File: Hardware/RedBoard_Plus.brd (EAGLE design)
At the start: 68.6 x 58.4 mm, 176 parts, among them IC3 LM1117, J2 ISP, J3 5.5x2.1mm Barrel, J4 QWIIC_RIGHT_ANGLE, J5 USB Female Type C Connector, Q1 20V/4.2A/52mΩ/1.4W, Q2 310mA/60V/1.6Ω, Q3 310mA/60V/1.6Ω, U1 CH340G, U3 3.3V, U4 ATMEGA328P_TQFP, Y1 16MHz, Y2 12MHz

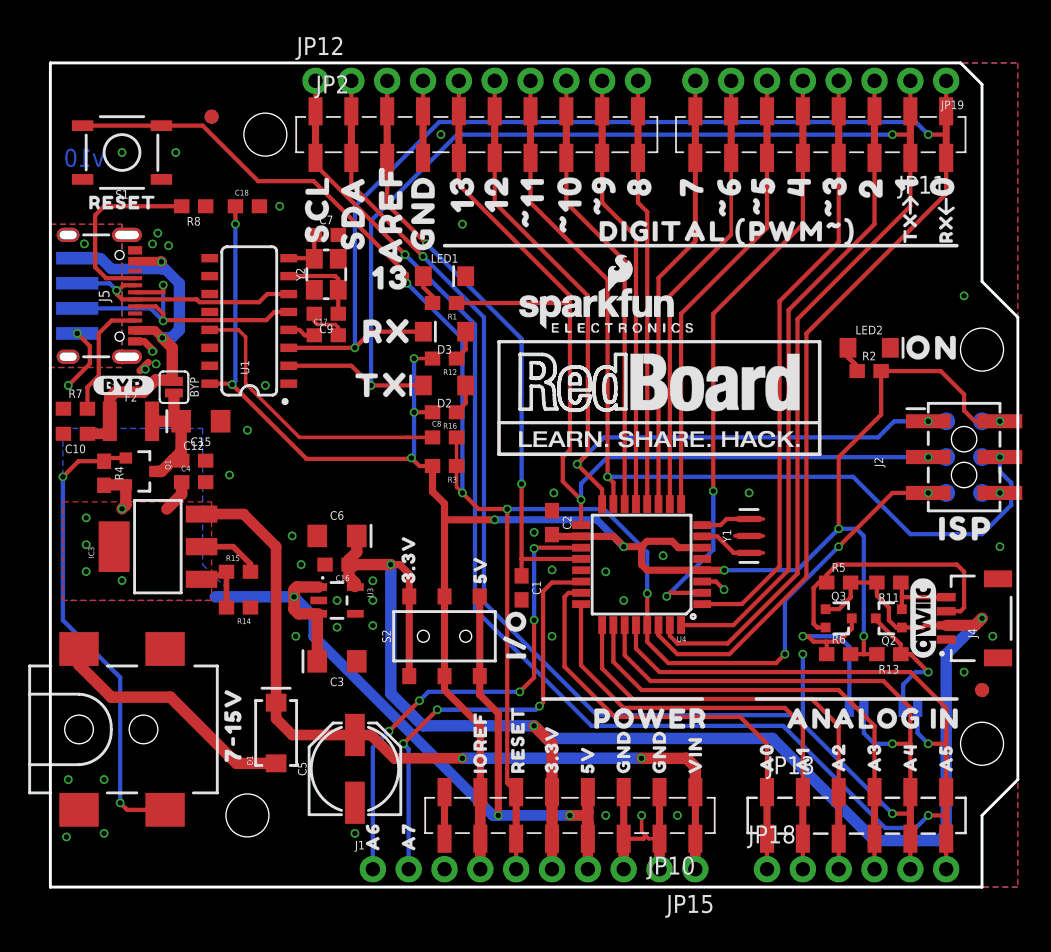
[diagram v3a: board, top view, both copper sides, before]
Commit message: Update silkscreen
Increased the size of PTH labels on back side to all be the same size
Added "(PLUS)" label to board name - top/bottom
Vector-ized "ELECTRONICS"
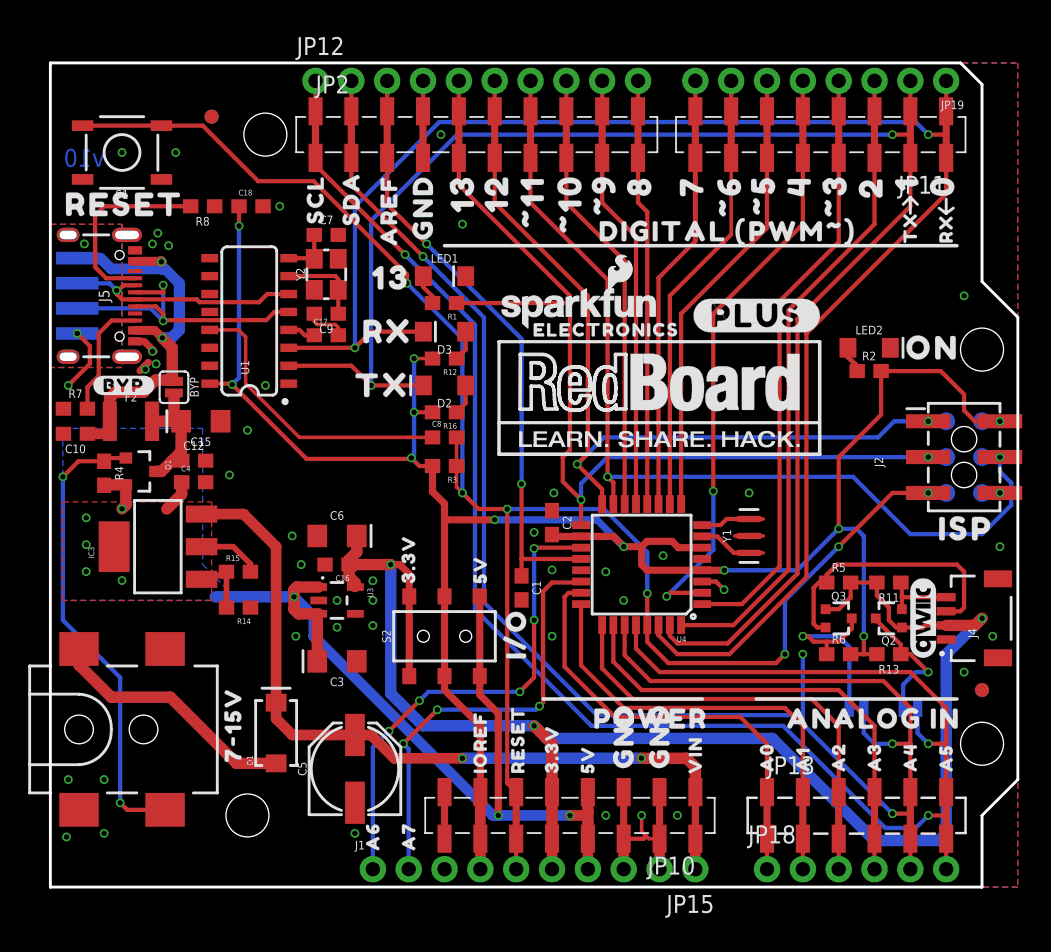
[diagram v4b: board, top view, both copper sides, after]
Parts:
- added U$102: (no value), output:_A50
- added U$103: (no value), output:#PLUS#0
- added U$104: (no value), output:ELECTRONICS0
- U$100: device output:_GND0 -> output:#PLUS#0
- U$13: device output:RESET0 -> output:_RESET0
- U$18: device output:SCL0 -> output:_AREF0
- U$19: device output:SDA0 -> output:_SCL0
- U$20: device output:AREF0 -> output:_SDA0
- U$84: device output:A40 -> output:_A40
- U$86: device output:A50 -> output:_A30
- U$87: device output:A30 -> output:_A20
- U$88: device output:A20 -> output:_A10
- U$89: device output:A10 -> output:_A00
- U$90: device output:A00 -> output:_VIN0
- U$91: device output:VIN0 -> output:_GND0
- U$92: device output:GND0 -> output:_GND0
- U$93: device output:GND0 -> output:_5V0
- U$94: device output:5V0 -> output:_3#3V0
- U$95: device output:3#3V0 -> output:_RESET0
- U$96: device output:RESET0 -> output:_IOREF0
- U$97: device output:IOREF0 -> output:_A60
- U$98: device output:A70 -> output:_A70
- U$99: device output:A60 -> output:GND0
- moved U$99 39.9 mm to (26.4, 44.8), flipped to the top, turned to 90 degrees
- moved U$100 19.4 mm to (45.6, 40.5), turned to 0 degrees
- moved U$97 7.62 mm to (22.9, 7.62)
- moved U$95 6.60 mm to (33.0, 12.7)
- moved U$90 6.35 mm to (45.7, 8.89)
- moved U$94 5.68 mm to (35.6, 10.2)
- moved U$86 5.68 mm to (58.4, 7.62)
- moved U$18 5.09 mm to (24.0, 44.2)
- moved U$91 4.76 mm to (43.1, 9.65)
- moved U$96 4.69 mm to (30.5, 11.8)
- moved U$92 4.27 mm to (40.6, 9.65)
- moved U$20 3.78 mm to (21.3, 45.6)
- moved U$89 3.78 mm to (50.8, 7.62)
- moved U$87 3.59 mm to (55.9, 7.62)
- moved U$88 3.33 mm to (53.3, 7.24)
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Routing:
- net CC1: track 13.2 -> 13.9 mm

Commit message: Run checklist
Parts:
- moved JP7 1.27 mm to (39.1, 43.6)
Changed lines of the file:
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@@
 <?xml version="1.0" encoding="utf-8"?>
 <!DOCTYPE eagle SYSTEM "eagle.dtd">
-<eagle version="9.6.2">
+<eagle version="9.5.2">
 <drawing>
 <settings>
-<setting alwaysvectorfont="yes"/>
+<setting alwaysvectorfont="no"/>
 <setting keepoldvectorfont="yes"/>
 <setting verticaltext="up"/>
@@
 <wire x1="66.04" y1="56.896" x2="66.04" y2="42.926" width="0.2032" layer="20"/>
 <text x="0" y="-0.0635" size="0.0254" layer="214" font="vector">D:/SmartProjects/Snc/a4_bn_logo2.bmp</text>
-<text x="2.413" y="51.689" size="1.27" layer="16" font="vector" ratio="20" rot="MR0" align="center">v10</text>
+<text x="2.413" y="56.769" size="1.27" layer="16" font="vector" ratio="20" rot="MR0" align="center">v10</text>
 <rectangle x1="0.635" y1="22.352" x2="2.032" y2="30.607" layer="43"/>
 <rectangle x1="5.715" y1="23.114" x2="7.366" y2="30.607" layer="43"/>
@@
 </element>
 <element name="JP1" library="SparkFun-Aesthetics" package="SFE_LOGO_NAME_.1" value="SFE_LOGO_NAME.1_INCH" x="37.465" y="41.021" smashed="yes"/>
-<element name="JP7" library="SparkFun-Aesthetics" package="SFE_LOGO_FLAME_.1" value="SFE_LOGO_FLAME.1_INCH" x="40.386" y="43.561" smashed="yes"/>
+<element name="JP7" library="SparkFun-Aesthetics" package="SFE_LOGO_FLAME_.1" value="SFE_LOGO_FLAME.1_INCH" x="39.116" y="43.561" smashed="yes"/>
 <element name="J2" library="SparkFun-Connectors" package="2X3_SMT_POSTS" value="ISP" x="64.77" y="30.48" smashed="yes" rot="R270">
 <attribute name="NAME" x="58.42" y="30.48" size="0.6096" layer="25" rot="R270"/>
@@
 <contactref element="J5" pad="B6"/>
 <contactref element="J5" pad="A6"/>
-<wire x1="6.01" y1="42.16" x2="8.005" y2="42.16" width="0.3048" layer="1"/>
 <wire x1="6.01" y1="41.16" x2="7.481" y2="41.16" width="0.3048" layer="1"/>
 <wire x1="7.481" y1="41.16" x2="8.001" y2="40.64" width="0.3048" layer="1"/>
@@
 <wire x1="8.001" y1="40.132" x2="8.001" y2="42.672" width="0.3048" layer="16"/>
 <via x="8.001" y="42.672" extent="1-16" drill="0.381"/>
-<wire x1="8.001" y1="42.672" x2="8.005" y2="42.668" width="0.3048" layer="1"/>
-<wire x1="8.005" y1="42.668" x2="8.005" y2="42.16" width="0.3048" layer="1"/>
+<wire x1="8.001" y1="42.672" x2="7.489" y2="42.16" width="0.3048" layer="1"/>
+<wire x1="6.01" y1="42.16" x2="7.489" y2="42.16" width="0.3048" layer="1"/>
 <contactref element="JP14" pad="D+"/>
 <wire x1="7.112" y1="41.021" x2="8.001" y2="40.132" width="0.3048" layer="16"/>
@@
 <contactref element="R3" pad="1"/>
 <wire x1="42.31" y1="17.38" x2="43.815" y2="15.875" width="0.3048" layer="1"/>
-<wire x1="33.02" y1="6.73" x2="32.385" y2="7.365" width="0.3048" layer="1"/>
-<wire x1="32.385" y1="26.797" x2="32.385" y2="7.365" width="0.3048" layer="1"/>
+<wire x1="33.02" y1="6.73" x2="33.02" y2="8.762" width="0.3048" layer="1"/>
+<wire x1="33.02" y1="8.762" x2="32.385" y2="9.397" width="0.3048" layer="1"/>
+<wire x1="32.385" y1="26.797" x2="32.385" y2="9.397" width="0.3048" layer="1"/>
 <wire x1="42.31" y1="20.809" x2="42.31" y2="18.5674" width="0.3048" layer="1"/>
 <wire x1="42.31" y1="23.73" x2="42.31" y2="20.809" width="0.3048" layer="16"/>

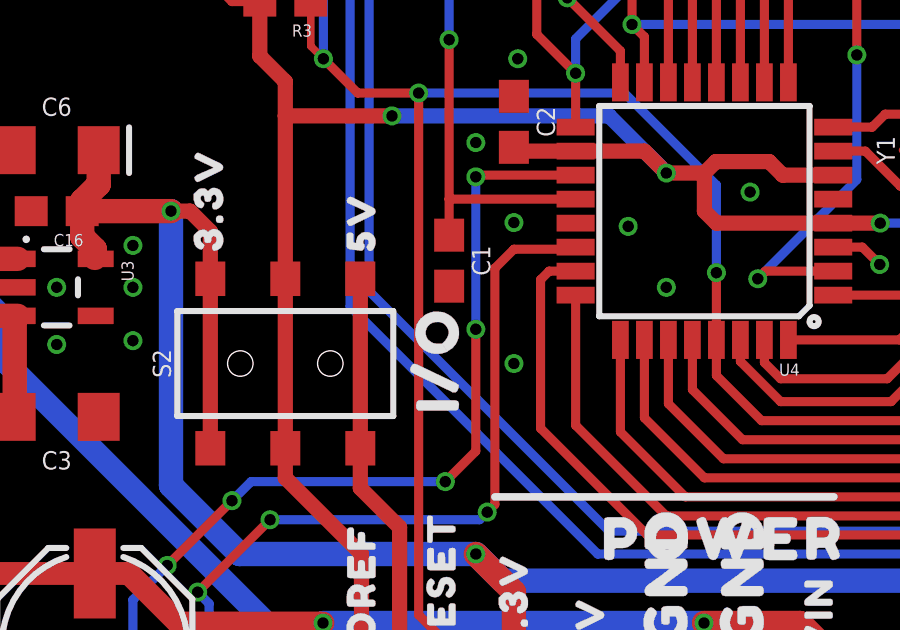
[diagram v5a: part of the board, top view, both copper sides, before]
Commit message: Change "I/O" label to "Logic" and make A4/A5 jumper labels inverted pill-shape
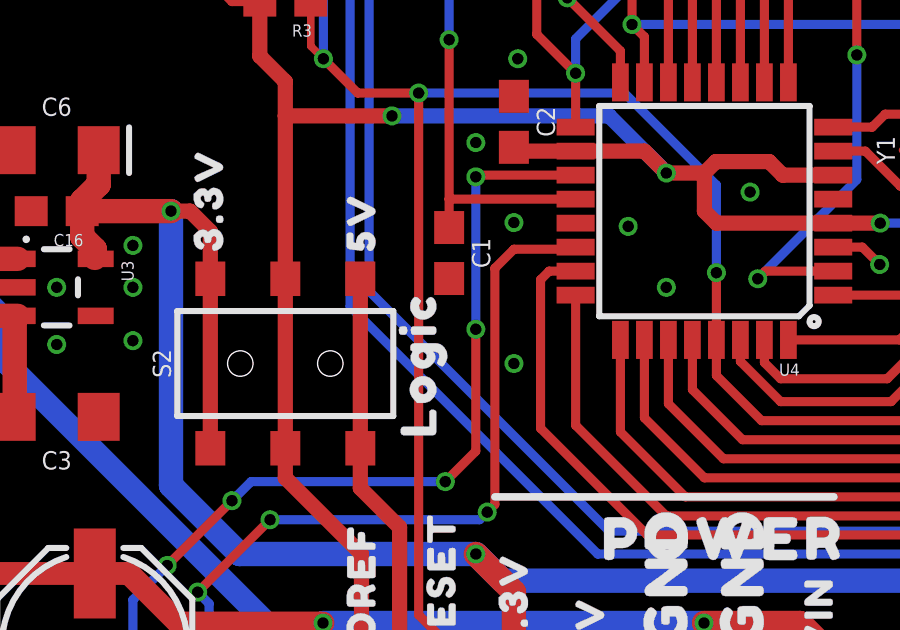
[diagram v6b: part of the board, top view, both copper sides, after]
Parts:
- removed U$42: (no value), output:I#O0
- removed U$85: (no value), output:A50
- added U$105: (no value), output:#A4#0
- added U$106: (no value), output:#A5#0
- U$11: device output:A40 -> output:LOGIC0
- moved U$11 26.5 mm to (32.4, 14.5), flipped to the top, turned to 90 degrees
- moved C1 0.25 mm to (33.4, 21.5)
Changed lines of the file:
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@@
 <?xml version="1.0" encoding="utf-8"?>
 <!DOCTYPE eagle SYSTEM "eagle.dtd">
-<eagle version="9.5.2">
+<eagle version="9.6.2">
 <drawing>
 <settings>
-<setting alwaysvectorfont="no"/>
+<setting alwaysvectorfont="yes"/>
 <setting keepoldvectorfont="yes"/>
 <setting verticaltext="up"/>
@@
 </autorouter>
 <elements>
-<element name="C1" library="SparkFun-Capacitors" package="0603" value="0.1uF" x="33.401" y="21.209" smashed="yes" rot="R270">
-<attribute name="NAME" x="34.163" y="21.209" size="0.6096" layer="25" font="vector" ratio="20" rot="R270" align="bottom-center"/>
-<attribute name="PROD_ID" value="CAP-00810" x="33.401" y="21.209" size="1.778" layer="27" rot="R270" display="off"/>
-<attribute name="VALUE" x="32.639" y="21.209" size="0.6096" layer="27" font="vector" ratio="15" rot="R270" align="top-center"/>
+<element name="C1" library="SparkFun-Capacitors" package="0603" value="0.1uF" x="33.401" y="21.463" smashed="yes" rot="R270">
+<attribute name="NAME" x="34.163" y="21.463" size="0.6096" layer="25" font="vector" ratio="20" rot="R270" align="bottom-center"/>
+<attribute name="PROD_ID" value="CAP-00810" x="33.401" y="21.463" size="1.778" layer="27" rot="R270" display="off"/>
+<attribute name="VALUE" x="32.639" y="21.463" size="0.6096" layer="27" font="vector" ratio="15" rot="R270" align="top-center"/>
 </element>
 <element name="R1" library="SparkFun-Resistors" package="0603" value="4.7k" x="27.94" y="41.402" smashed="yes" rot="R180">
@@
 <element name="U$43" library="output" package="3#3V0" value="" x="25.4" y="20.828" smashed="yes" rot="R90"/>
 <element name="U$44" library="output" package="5V0" value="" x="30.48" y="20.828" smashed="yes" rot="R90"/>
-<element name="U$42" library="output" package="I#O0" value="" x="33.02" y="15.113" smashed="yes" rot="R90"/>
 <element name="U$45" library="output" package="ON0" value="" x="59.436" y="38.227" smashed="yes"/>
 <element name="U$46" library="output" package="ISP0" value="" x="61.722" y="25.4" smashed="yes"/>
@@
 <element name="U$2" library="output" package="_D#0" value="" x="6.096" y="42.799" smashed="yes" rot="MR0"/>
 <element name="U$10" library="output" package="G0" value="" x="5.207" y="39.243" smashed="yes" rot="MR0"/>
-<element name="U$11" library="output" package="A40" value="" x="58.928" y="14.478" smashed="yes" rot="MR0"/>
-<element name="U$85" library="output" package="A50" value="" x="62.611" y="14.478" smashed="yes" rot="MR0"/>
 <element name="U$21" library="output" package="_GND0" value="" x="26.416" y="57.658" smashed="yes" rot="MR270"/>
 <element name="FD1" library="SparkFun-Aesthetics" package="FIDUCIAL-1X2" value="FIDUCIAL1X2" x="11.43" y="54.61" smashed="yes" rot="MR0"/>
@@
 <element name="U$103" library="output" package="#PLUS#0" value="" x="49.022" y="50.292" smashed="yes" rot="MR0"/>
 <element name="U$104" library="output" package="ELECTRONICS0" value="" x="33.528" y="39.497" smashed="yes"/>
+<element name="U$105" library="output" package="#A4#0" value="" x="58.801" y="14.732" smashed="yes" rot="MR0"/>
+<element name="U$106" library="output" package="#A5#0" value="" x="62.611" y="14.732" smashed="yes" rot="MR0"/>
+<element name="U$11" library="output" package="LOGIC0" value="" x="32.385" y="14.478" smashed="yes" rot="R90"/>
 </elements>
 <signals>
@@
 <wire x1="33.401" y1="28.575" x2="33.401" y2="38.862" width="0.3048" layer="16"/>
 <contactref element="U4" pad="20"/>
-<wire x1="33.401" y1="22.059" x2="33.401" y2="23.26" width="0.3048" layer="1"/>
+<wire x1="33.401" y1="22.313" x2="33.401" y2="23.26" width="0.3048" layer="1"/>
 <wire x1="23.876" y1="51.69" x2="23.876" y2="48.387" width="0.3048" layer="1"/>
 <wire x1="23.876" y1="48.387" x2="26.67" y2="45.593" width="0.3048" layer="1"/>

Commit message: Add "DNP" to headers on schematic
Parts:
- J1, JP15, JP18, JP19: value (none) -> DNP
- JP12: value M10NO_SILK -> DNP
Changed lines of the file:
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@@
 <?xml version="1.0" encoding="utf-8"?>
 <!DOCTYPE eagle SYSTEM "eagle.dtd">
-<eagle version="9.6.2">
+<eagle version="9.5.2">
 <drawing>
 <settings>
-<setting alwaysvectorfont="yes"/>
+<setting alwaysvectorfont="no"/>
 <setting keepoldvectorfont="yes"/>
 <setting verticaltext="up"/>
@@
 <attribute name="REV" value="" x="-5.08" y="-35.56" size="1.778" layer="27" font="vector" ratio="15" display="off"/>
 </element>
-<element name="JP12" library="SparkFun-Connectors" package="1X10_NO_SILK" value="M10NO_SILK" x="18.796" y="57.15" smashed="yes">
+<element name="JP12" library="SparkFun-Connectors" package="1X10_NO_SILK" value="DNP" x="18.796" y="57.15" smashed="yes">
 <attribute name="NAME" x="17.4498" y="58.9788" size="1.27" layer="25" ratio="10"/>
 <attribute name="PROD_ID" value="CONN-11219" x="18.796" y="57.15" size="1.778" layer="27" font="vector" ratio="15" display="off"/>
 <attribute name="VALUE" x="17.526" y="53.975" size="1.27" layer="27"/>
 </element>
-<element name="JP15" library="SparkFun-Connectors" package="1X08_NO_SILK@1" value="" x="45.72" y="1.27" smashed="yes" rot="R180">
+<element name="JP15" library="SparkFun-Connectors" package="1X08_NO_SILK@1" value="DNP" x="45.72" y="1.27" smashed="yes" rot="R180">
 <attribute name="NAME" x="47.0662" y="-0.5588" size="1.27" layer="25" ratio="10" rot="R180"/>
 <attribute name="PROD_ID" value="CONN-10204" x="45.72" y="1.27" size="1.778" layer="27" font="vector" ratio="15" rot="R180" display="off"/>
 <attribute name="VALUE" x="46.99" y="4.445" size="1.27" layer="27" rot="R180"/>
 </element>
-<element name="JP18" library="SparkFun-Connectors" package="1X06_NO_SILK@1" value="" x="50.8" y="1.27" smashed="yes">
+<element name="JP18" library="SparkFun-Connectors" package="1X06_NO_SILK@1" value="DNP" x="50.8" y="1.27" smashed="yes">
 <attribute name="NAME" x="49.4538" y="3.0988" size="1.27" layer="25" ratio="10"/>
 <attribute name="PROD_ID" value="CONN-10203" x="50.8" y="1.27" size="1.778" layer="27" font="vector" ratio="15" display="off"/>
 <attribute name="VALUE" x="49.53" y="-1.905" size="1.27" layer="27"/>
 </element>
-<element name="JP19" library="SparkFun-Connectors" package="1X08_NO_SILK" value="" x="63.5" y="57.15" smashed="yes" rot="R180">
+<element name="JP19" library="SparkFun-Connectors" package="1X08_NO_SILK" value="DNP" x="63.5" y="57.15" smashed="yes" rot="R180">
 <attribute name="NAME" x="64.77" y="55.753" size="0.6096" layer="25" font="vector" ratio="20" rot="R180"/>
 <attribute name="PROD_ID" value="CONN-08438" x="63.5" y="57.15" size="1.778" layer="27" font="vector" ratio="15" rot="R180" display="off"/>
 <attribute name="VALUE" x="64.77" y="59.182" size="0.6096" layer="27" font="vector" ratio="20" rot="R180"/>
 </element>
-<element name="J1" library="SparkFun-Connectors" package="1X02_NO_SILK" value="" x="22.86" y="1.27" smashed="yes">
+<element name="J1" library="SparkFun-Connectors" package="1X02_NO_SILK" value="DNP" x="22.86" y="1.27" smashed="yes">
 <attribute name="NAME" x="21.59" y="2.667" size="0.6096" layer="25" font="vector" ratio="20"/>
 <attribute name="VALUE" x="21.59" y="-0.762" size="0.6096" layer="27" font="vector" ratio="20"/>

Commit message: QC Double check changes
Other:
- board text added: "Revised By: Priyanka Makin"
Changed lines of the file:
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@@
 <text x="26.67" y="-39.37" size="1.778" layer="51" font="vector" ratio="15">Jim Lindblom
 N. Seidle</text>
+<text x="6.35" y="-41.91" size="1.778" layer="51" font="vector" ratio="15">Revised By: Priyanka Makin</text>
 </plain>
 <attributes>
@@
 <via x="35.56" y="22.479" extent="1-16" drill="0.381"/>
 <via x="34.29" y="25.146" extent="1-16" drill="0.381"/>
-<wire x1="1.27" y1="35.56" x2="1.397" y2="35.56" width="0.254" layer="1"/>
 <via x="1.905" y="39.243" extent="1-16" drill="0.381"/>
 <wire x1="1.905" y1="39.243" x2="2.794" y2="38.354" width="0.3048" layer="1"/>
@@
 <contactref element="Y2" pad="2"/>
 <contactref element="Y2" pad="4"/>
-<wire x1="20.232" y1="39.116" x2="20.408" y2="39.116" width="0.3048" layer="1"/>
 <wire x1="18.708" y1="40.64" x2="18.708" y2="40.093" width="0.254" layer="1"/>
 <wire x1="18.923" y1="39.878" x2="20.193" y2="39.878" width="0.254" layer="1"/>
